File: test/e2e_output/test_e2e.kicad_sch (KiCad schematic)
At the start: 3 parts, among them U1 CP_Radial_D25.0mm_P10.00mm_Sn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, U2 R_Axial_DIN0207_L6.3mm_D2.5mm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, U3 R_Axial_DIN0207_L6.3mm_D2.5mm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

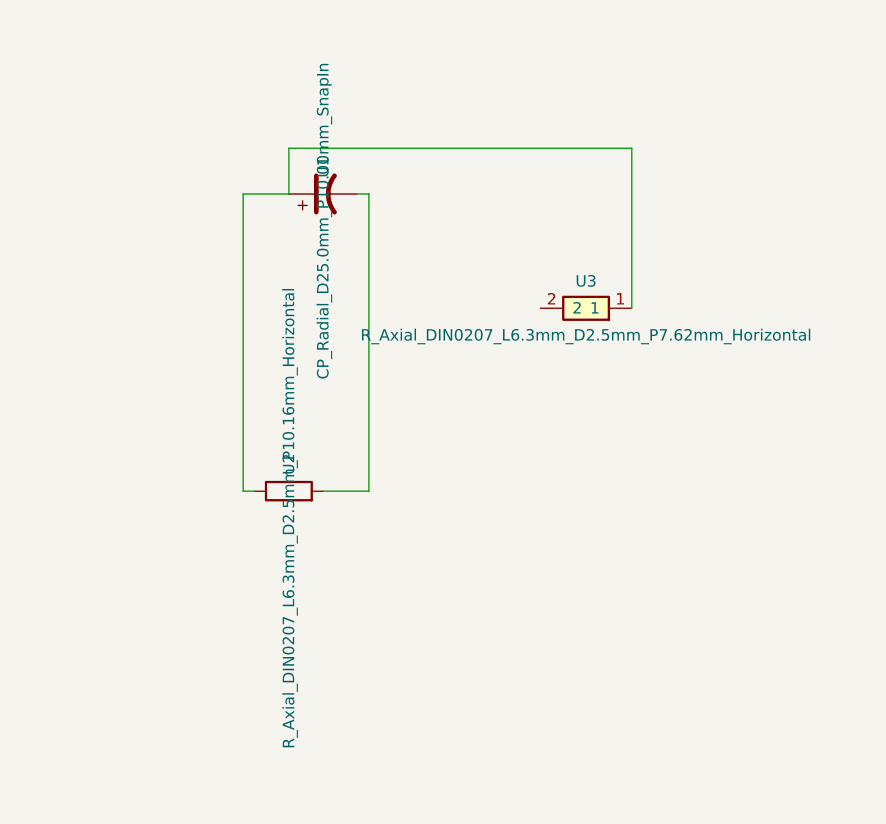
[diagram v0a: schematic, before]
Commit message: fix: schematic router - pin_map mapping + rotation formula alignment
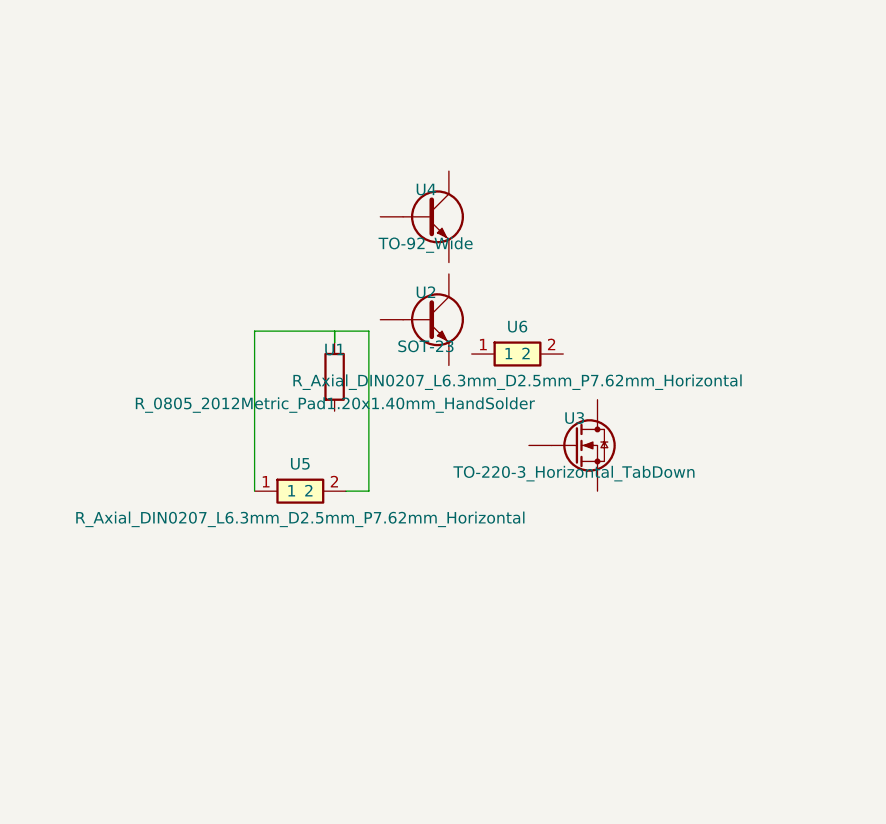
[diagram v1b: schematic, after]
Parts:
- removed U1: CP_Radial_D25.0mm_P10.00mm_SnapIn, 00_basic:CP_Radial_D25.0mm_P10.00mm_SnapIn, symbol 00_basic:C_Polarized
- removed U2: R_Axial_DIN0207_L6.3mm_D2.5mm_P10.16mm_Horizontal, 00_basic:R_Axial_DIN0207_L6.3mm_D2.5mm_P10.16mm_Horizontal, symbol 00_basic:R
- removed U3: R_Axial_DIN0207_L6.3mm_D2.5mm_P7.62mm_Horizontal, 00_basic:R_Axial_DIN0207_L6.3mm_D2.5mm_P7.62mm_Horizontal, symbol _placeholder:U3
- added U1: R_0805_2012Metric_Pad1.20x1.40mm_HandSolder, 00_basic:R_0805_2012Metric_Pad1.20x1.40mm_HandSolder, symbol RE_passive:R
- added U2: SOT-23, RE_active:SOT-23, symbol RE_active:Q_NPN
- added U3: TO-220-3_Horizontal_TabDown, RE_active:TO-220-3_Horizontal_TabDown, symbol RE_active:Q_NMOS
- added U4: TO-92_Wide, RE_active:TO-92_Wide, symbol RE_active:Q_NPN
- added U5: R_Axial_DIN0207_L6.3mm_D2.5mm_P7.62mm_Horizontal, RE_passive_tht:R_Axial_DIN0207_L6.3mm_D2.5mm_P7.62mm_Horizontal, symbol _placeholder:U5
- added U6: R_Axial_DIN0207_L6.3mm_D2.5mm_P7.62mm_Horizontal, RE_passive_tht:R_Axial_DIN0207_L6.3mm_D2.5mm_P7.62mm_Horizontal, symbol _placeholder:U6
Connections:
- new net: U1.1, U5.1, U5.2
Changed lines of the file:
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@@
   (paper "A4")
   (symbol
-    (lib_id "00_basic:C_Polarized")
-    (at 135.89 88.90 90)
+    (lib_id "RE_passive:R")
+    (at 137.16 109.22 0)
     (unit 1)
     (exclude_from_sim no)
@@
     (on_board yes)
     (dnp no)
-    (property "Reference" "U1" (at 135.89 85.90 0)
+    (property "Reference" "U1" (at 137.16 106.22 0)
       (effects (font (size 1.27 1.27)))
     )
-    (property "Value" "CP_Radial_D25.0mm_P10.00mm_SnapIn" (at 135.89 91.90 0)
+    (property "Value" "R_0805_2012Metric_Pad1.20x1.40mm_HandSolder" (at 137.16 112.22 0)
       (effects (font (size 1.27 1.27)))
     )
-    (property "Footprint" "00_basic:CP_Radial_D25.0mm_P10.00mm_SnapIn" (at 135.89 93.90 0)
+    (property "Footprint" "00_basic:R_0805_2012Metric_Pad1.20x1.40mm_HandSolder" (at 137.16 114.22 0)
       (effects (font (size 1.27 1.27)) hide)
     )
@@
   )
   (symbol
-    (lib_id "00_basic:R")
-    (at 132.08 121.92 90)
+    (lib_id "RE_active:Q_NPN")
+    (at 147.32 102.87 0)
     (unit 1)
     (exclude_from_sim no)
@@
     (on_board yes)
     (dnp no)
-    (property "Reference" "U2" (at 132.08 118.92 0)
+    (property "Reference" "U2" (at 147.32 99.87 0)
       (effects (font (size 1.27 1.27)))
     )
-    (property "Value" "R_Axial_DIN0207_L6.3mm_D2.5mm_P10.16mm_Horizontal" (at 132.08 124.92 0)
+    (property "Value" "SOT-23" (at 147.32 105.87 0)
       (effects (font (size 1.27 1.27)))
     )
-    (property "Footprint" "00_basic:R_Axial_DIN0207_L6.3mm_D2.5mm_P10.16mm_Horizontal" (at 132.08 126.92 0)
+    (property "Footprint" "RE_active:SOT-23" (at 147.32 107.87 0)
       (effects (font (size 1.27 1.27)) hide)
     )
@@
   )
   (symbol
-    (lib_id "_placeholder:U3")
-    (at 165.10 101.60 180)
+    (lib_id "RE_active:Q_NMOS")
+    (at 163.83 116.84 0)
     (unit 1)
     (exclude_from_sim no)
@@
     (on_board yes)
     (dnp no)
-    (property "Reference" "U3" (at 165.10 98.60 0)
+    (property "Reference" "U3" (at 163.83 113.84 0)
       (effects (font (size 1.27 1.27)))
     )
-    (property "Value" "R_Axial_DIN0207_L6.3mm_D2.5mm_P7.62mm_Horizontal" (at 165.10 104.60 0)
+    (property "Value" "TO-220-3_Horizontal_TabDown" (at 163.83 119.84 0)
       (effects (font (size 1.27 1.27)))
     )
-    (property "Footprint" "00_basic:R_Axial_DIN0207_L6.3mm_D2.5mm_P7.62mm_Horizontal" (at 165.10 106.60 0)
+    (property "Footprint" "RE_active:TO-220-3_Horizontal_TabDown" (at 163.83 121.84 0)
       (effects (font (size 1.27 1.27)) hide)
     )
@@
     )
   )
-  (wire (pts (xy 139.70 88.90) (xy 140.97 88.90))
+  (symbol
+    (lib_id "RE_active:Q_NPN")
+    (at 147.32 91.44 0)
+    (unit 1)
+    (exclude_from_sim no)
+    (in_bom yes)
+    (on_board yes)
+    (dnp no)
+    (property "Reference" "U4" (at 147.32 88.44 0)
+      (effects (font (size 1.27 1.27)))
+    )
+    (property "Value" "TO-92_Wide" (at 147.32 94.44 0)
+      (effects (font (size 1.27 1.27)))
+    )
+    (property "Footprint" "RE_active:TO-92_Wide" (at 147.32 96.44 0)
+      (effects (font (size 1.27 1.27)) hide)
+    )
+    (instances
+      (project ""
+        (path "/"
+          (reference "U4")
+          (unit 1)
+        )
+      )
+    )
+  )
+  (symbol
+    (lib_id "_placeholder:U5")
+    (at 133.35 121.92 0)
+    (unit 1)
+    (exclude_from_sim no)
+    (in_bom yes)
+    (on_board yes)
+    (dnp no)
+    (property "Reference" "U5" (at 133.35 118.92 0)
+      (effects (font (size 1.27 1.27)))
+    )
+    (property "Value" "R_Axial_DIN0207_L6.3mm_D2.5mm_P7.62mm_Horizontal" (at 133.35 124.92 0)
+      (effects (font (size 1.27 1.27)))
+    )
+    (property "Footprint" "RE_passive_tht:R_Axial_DIN0207_L6.3mm_D2.5mm_P7.62mm_Horizontal" (at 133.35 126.92 0)
+      (effects (font (size 1.27 1.27)) hide)
+    )
+    (instances
+      (project ""
+        (path "/"
+          (reference "U5")
+          (unit 1)
+        )
+      )
+    )
+  )
+  (symbol
+    (lib_id "_placeholder:U6")
+    (at 157.48 106.68 0)
+    (unit 1)
+    (exclude_from_sim no)
+    (in_bom yes)
+    (on_board yes)
+    (dnp no)
+    (property "Reference" "U6" (at 157.48 103.68 0)
+      (effects (font (size 1.27 1.27)))
+    )
+    (property "Value" "R_Axial_DIN0207_L6.3mm_D2.5mm_P7.62mm_Horizontal" (at 157.48 109.68 0)
+      (effects (font (size 1.27 1.27)))
+    )
+    (property "Footprint" "RE_passive_tht:R_Axial_DIN0207_L6.3mm_D2.5mm_P7.62mm_Horizontal" (at 157.48 111.68 0)
+      (effects (font (size 1.27 1.27)) hide)
+    )
+    (instances
+      (project ""
+        (path "/"
+          (reference "U6")
+          (unit 1)
+        )
+      )
+    )
+  )
+  (wire (pts (xy 138.43 121.92) (xy 140.97 121.92))
     (stroke (width 0) (type default))
   )
-  (wire (pts (xy 140.97 88.90) (xy 140.97 121.92))
+  (wire (pts (xy 140.97 121.92) (xy 140.97 104.14))
     (stroke (width 0) (type default))
   )
-  (wire (pts (xy 140.97 121.92) (xy 135.89 121.92))
+  (wire (pts (xy 140.97 104.14) (xy 137.16 104.14))
     (stroke (width 0) (type default))
   )
-  (wire (pts (xy 132.08 88.90) (xy 127.00 88.90))
+  (wire (pts (xy 137.16 104.14) (xy 137.16 105.41))
     (stroke (width 0) (type default))
   )
-  (wire (pts (xy 127.00 88.90) (xy 127.00 121.92))
+  (wire (pts (xy 128.27 121.92) (xy 128.27 104.14))
     (stroke (width 0) (type default))
   )
-  (wire (pts (xy 127.00 121.92) (xy 128.27 121.92))
+  (wire (pts (xy 128.27 104.14) (xy 137.16 104.14))
     (stroke (width 0) (type default))
   )
-  (wire (pts (xy 132.08 88.90) (xy 132.08 83.82))
+  (wire (pts (xy 137.16 104.14) (xy 137.16 105.41))
     (stroke (width 0) (type default))
   )
-  (wire (pts (xy 132.08 83.82) (xy 170.18 83.82))
-    (stroke (width 0) (type default))
-  )
-  (wire (pts (xy 170.18 83.82) (xy 170.18 101.60))
-    (stroke (width 0) (type default))
-  )

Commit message: backup
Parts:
- added U7: CP_Radial_D30.0mm_P10.00mm_SnapIn, RE_passive_tht:CP_Radial_D30.0mm_P10.00mm_SnapIn, symbol RE_passive:C_Polarized
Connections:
- net at U1.1, U5.1, U5.2: now also U2.C, U3.D, U4.B, U4.C, U4.E
- net at U3.G: now also U7.2
